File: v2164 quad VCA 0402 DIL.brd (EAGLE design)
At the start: 41.3 x 14.6 mm, 45 parts, among them IC1 TL072JD, IC2 TL072JD, Q1 BA854SW

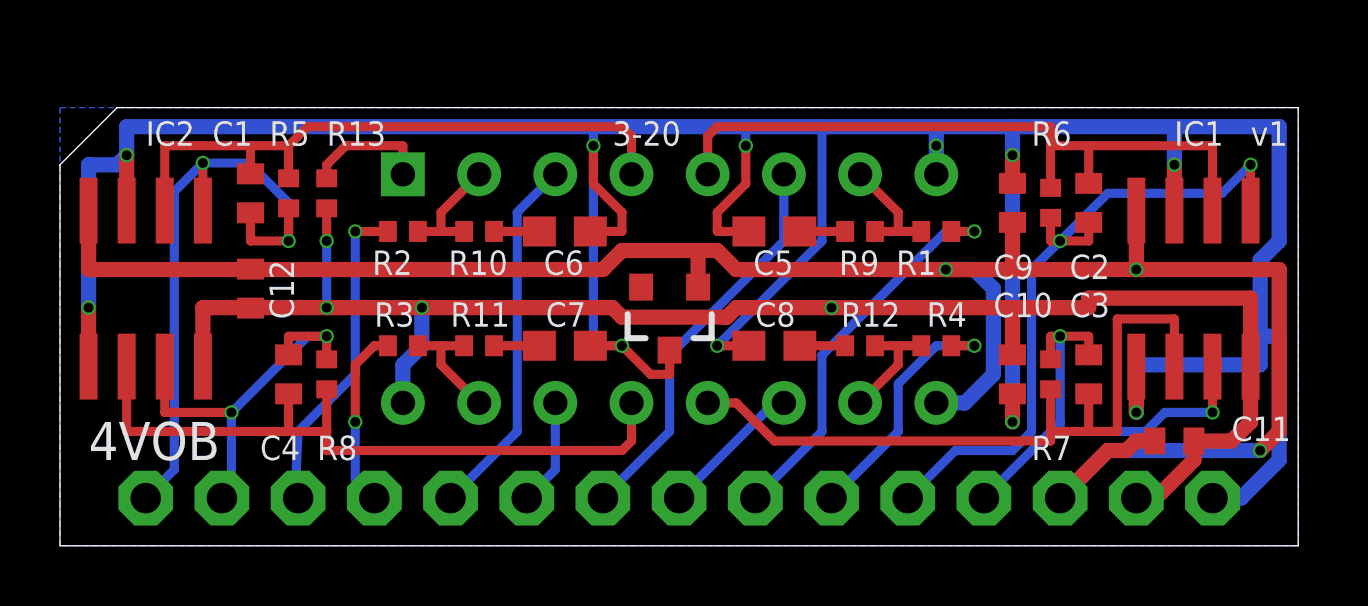
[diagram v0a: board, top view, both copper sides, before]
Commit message: Fixed some silk screen errors and replaced pads with some that solder slightly better
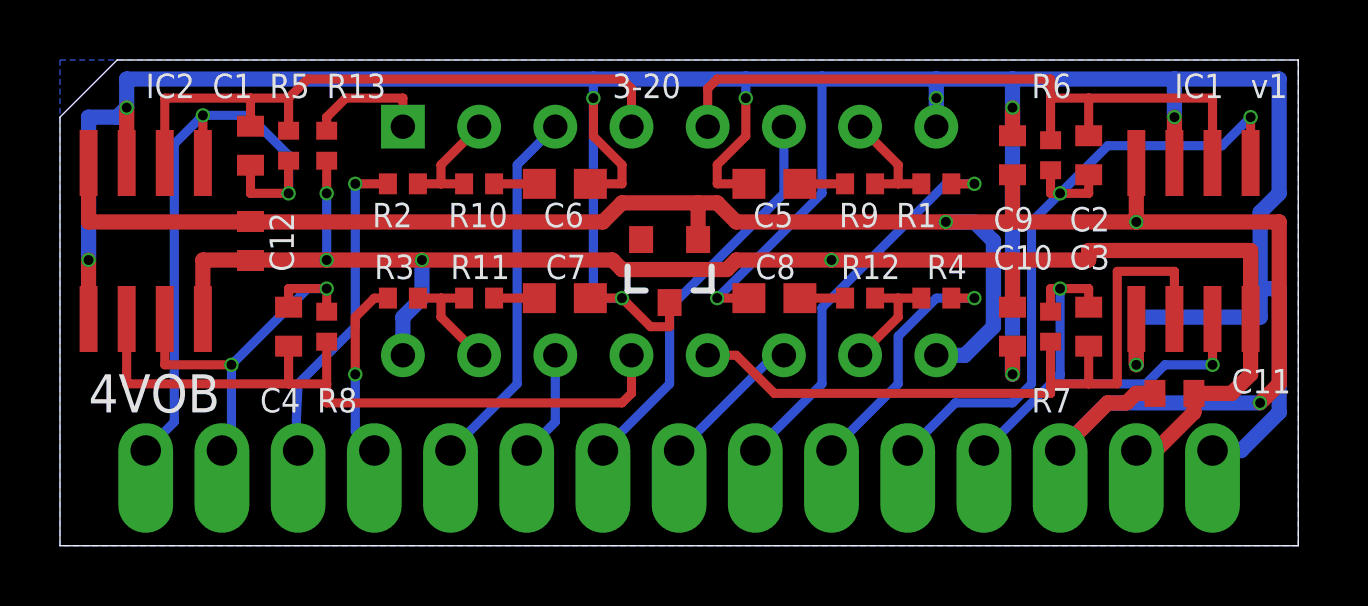
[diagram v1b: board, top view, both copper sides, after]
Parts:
- +15V, -15V, CV1, CV2, CV3, CV4, GND, IN1, IN2, IN3, IN4, OUT1, OUT2, OUT3, OUT4: device joakim:MA01N-1J -> joakim:SIP-PIN01-1J
- moved C1 1.59 mm to (6.35, 13.3)
- moved C10 1.59 mm to (31.8, 7.30)
- moved C12 1.59 mm to (6.35, 10.2)
- moved C2 1.59 mm to (34.3, 13.0)
- moved C3 1.59 mm to (34.3, 7.30)
- moved C4 1.59 mm to (7.62, 7.30)
- moved C5 1.59 mm to (23.8, 12.1)
- moved C6 1.59 mm to (16.8, 12.1)
- moved C7 1.59 mm to (16.8, 8.26)
- moved C8 1.59 mm to (23.8, 8.26)
- moved C9 1.59 mm to (31.8, 13.0)
- moved DA1 1.59 mm to (20.3, 10.2)
- moved IC1 1.59 mm to (37.8, 10.2)
- moved IC2 1.59 mm to (2.86, 10.2)
- moved R1 1.59 mm to (29.2, 12.1)
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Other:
- board size 41.3 x 14.6 mm -> 41.3 x 16.2 mm
- board text added: "Mount socket on this side!"

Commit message: Changed diode to B5817 (1n5817) as BAT854 is not available at JLCPCB
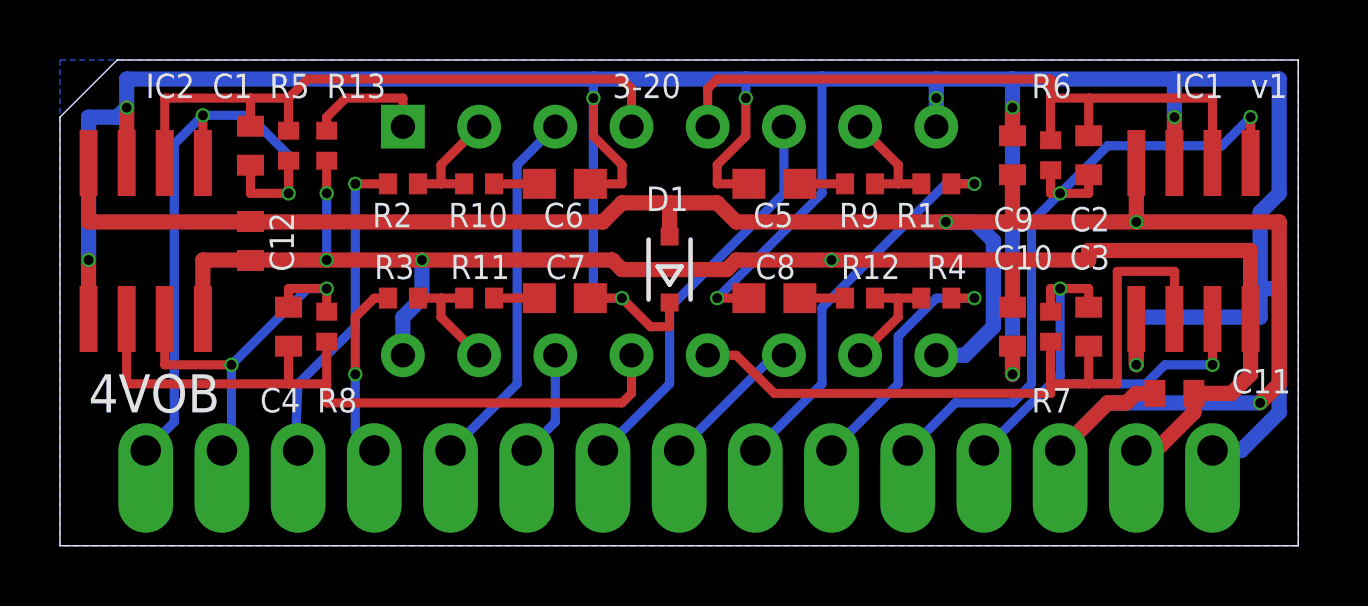
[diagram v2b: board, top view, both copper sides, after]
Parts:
- removed Q1: BA854SW, joakim:SOT23-3J
- added D1: B5817, diode:SOD323-R
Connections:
- net -15V: now also D1.A; no longer Q1.1
- net GND: now also D1.C; no longer Q1.3
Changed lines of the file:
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@@
 <layer number="2" name="Route2" color="16" fill="1" visible="no" active="no"/>
 <layer number="15" name="Route15" color="23" fill="1" visible="no" active="no"/>
-<layer number="16" name="Bottom" color="1" fill="1" visible="yes" active="yes"/>
+<layer number="16" name="Bottom" color="1" fill="1" visible="no" active="yes"/>
 <layer number="17" name="Pads" color="2" fill="1" visible="yes" active="yes"/>
 <layer number="18" name="Vias" color="2" fill="1" visible="yes" active="yes"/>
@@
 <attribute name="VALUE" x="4.445" y="10.795" size="1.27" layer="27" rot="R270"/>
 </element>
-<element name="Q1" library="joakim" package="SOT23-3J" value="BA854SW" x="20.32" y="9.2075" smashed="yes" rot="R180">
-<attribute name="VALUE" x="21.336" y="9.398" size="0.4064" layer="27" rot="R180"/>
-</element>
 <element name="U$1" library="joakim" package="XONIK_LOGO_18" value="" x="29.5275" y="8.3111" smashed="yes" rot="MR0"/>
+<element name="D1" library="diode" library_urn="urn:adsk.eagle:library:210" package="SOD323-R" package3d_urn="urn:adsk.eagle:package:43437/1" value="B5817" x="20.32" y="9.2075" smashed="yes" rot="R90">
+<attribute name="NAME" x="19.5375" y="11.16" size="0.8128" layer="25" font="vector"/>
+<attribute name="POPULARITY" value="4" x="20.32" y="9.2075" size="0.8128" layer="27" font="vector" rot="R90" display="off"/>
+<attribute name="VALUE" x="22.62" y="8.1075" size="1.27" layer="27" rot="R90"/>
+</element>
 </elements>
 <signals>
@@
 <wire x1="40.64" y1="8.5725" x2="40.005" y2="8.5725" width="0.508" layer="16"/>
 <wire x1="35.8775" y1="7.62" x2="35.8775" y2="6.0325" width="0.508" layer="16"/>
-<contactref element="Q1" pad="3"/>
 <wire x1="17.6775" y1="12.065" x2="18.7325" y2="12.065" width="0.3048" layer="1"/>
 <wire x1="18.7325" y1="12.065" x2="18.7325" y2="12.7" width="0.3048" layer="1"/>
@@
 <wire x1="21.9075" y1="12.7" x2="22.86" y2="13.6525" width="0.3048" layer="1"/>
 <via x="22.86" y="14.9225" extent="1-16" drill="0.3302"/>
-<wire x1="20.32" y1="8.1075" x2="20.32" y2="7.3025" width="0.3048" layer="1"/>
-<wire x1="20.32" y1="7.3025" x2="19.685" y2="7.3025" width="0.3048" layer="1"/>
-<wire x1="19.685" y1="7.3025" x2="18.7325" y2="8.255" width="0.3048" layer="1"/>
+<wire x1="18.7325" y1="8.255" x2="19.685" y2="7.3025" width="0.3048" layer="1"/>
 <wire x1="22.86" y1="13.6525" x2="22.86" y2="14.9225" width="0.3048" layer="1"/>
+<contactref element="D1" pad="C"/>
+<wire x1="19.685" y1="7.3025" x2="20.32" y2="7.3025" width="0.3048" layer="1"/>
+<wire x1="20.32" y1="7.3025" x2="20.32" y2="8.1075" width="0.3048" layer="1"/>
 </signal>
 <signal name="N$1">
@@
 <wire x1="29.5275" y1="10.795" x2="22.5425" y2="10.795" width="0.508" layer="1"/>
 <wire x1="22.5425" y1="10.795" x2="21.9075" y2="11.43" width="0.508" layer="1"/>
-<wire x1="21.9075" y1="11.43" x2="21.2725" y2="11.43" width="0.508" layer="1"/>
-<wire x1="21.2725" y1="11.43" x2="18.7325" y2="11.43" width="0.508" layer="1"/>
+<wire x1="20.32" y1="11.43" x2="18.7325" y2="11.43" width="0.508" layer="1"/>
 <wire x1="18.7325" y1="11.43" x2="18.0975" y2="10.795" width="0.508" layer="1"/>
 <wire x1="18.0975" y1="10.795" x2="6.35" y2="10.795" width="0.508" layer="1"/>
@@
 <wire x1="40.64" y1="10.795" x2="35.8775" y2="10.795" width="0.508" layer="1"/>
 <wire x1="34.925" y1="4.7625" x2="33.3375" y2="3.175" width="0.508" layer="16"/>
-<contactref element="Q1" pad="1"/>
 <via x="35.8775" y="10.795" extent="1-16" drill="0.3302"/>
-<wire x1="21.27" y1="10.2075" x2="21.27" y2="11.4275" width="0.508" layer="1"/>
-<wire x1="21.27" y1="11.4275" x2="21.2725" y2="11.43" width="0.508" layer="1"/>
+<contactref element="D1" pad="A"/>
+<wire x1="20.32" y1="10.3075" x2="20.32" y2="11.43" width="0.508" layer="1"/>
+<wire x1="21.9075" y1="11.43" x2="20.32" y2="11.43" width="0.508" layer="1"/>
 </signal>
 <signal name="OUT4">

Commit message: Tiny placement tweak
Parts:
- moved D1 0.32 mm to (20.3, 9.53)
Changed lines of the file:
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@@
 </element>
 <element name="U$1" library="joakim" package="XONIK_LOGO_18" value="" x="29.5275" y="8.3111" smashed="yes" rot="MR0"/>
-<element name="D1" library="diode" library_urn="urn:adsk.eagle:library:210" package="SOD323-R" package3d_urn="urn:adsk.eagle:package:43437/1" value="B5817" x="20.32" y="9.2075" smashed="yes" rot="R90">
-<attribute name="NAME" x="19.5375" y="11.16" size="0.8128" layer="25" font="vector"/>
-<attribute name="POPULARITY" value="4" x="20.32" y="9.2075" size="0.8128" layer="27" font="vector" rot="R90" display="off"/>
-<attribute name="VALUE" x="22.62" y="8.1075" size="1.27" layer="27" rot="R90"/>
+<element name="D1" library="diode" library_urn="urn:adsk.eagle:library:210" package="SOD323-R" package3d_urn="urn:adsk.eagle:package:43437/1" value="B5817" x="20.32" y="9.525" smashed="yes" rot="R90">
+<attribute name="NAME" x="19.5375" y="11.4775" size="0.8128" layer="25" font="vector"/>
+<attribute name="POPULARITY" value="4" x="20.32" y="9.525" size="0.8128" layer="27" font="vector" rot="R90" display="off"/>
+<attribute name="VALUE" x="22.62" y="8.425" size="1.27" layer="27" rot="R90"/>
 </element>
 </elements>
@@
 <wire x1="21.9075" y1="12.7" x2="22.86" y2="13.6525" width="0.3048" layer="1"/>
 <via x="22.86" y="14.9225" extent="1-16" drill="0.3302"/>
-<wire x1="18.7325" y1="8.255" x2="19.685" y2="7.3025" width="0.3048" layer="1"/>
+<wire x1="18.7325" y1="8.255" x2="19.3675" y2="7.62" width="0.3048" layer="1"/>
 <wire x1="22.86" y1="13.6525" x2="22.86" y2="14.9225" width="0.3048" layer="1"/>
 <contactref element="D1" pad="C"/>
-<wire x1="19.685" y1="7.3025" x2="20.32" y2="7.3025" width="0.3048" layer="1"/>
-<wire x1="20.32" y1="7.3025" x2="20.32" y2="8.1075" width="0.3048" layer="1"/>
+<wire x1="19.3675" y1="7.62" x2="20.32" y2="7.62" width="0.3048" layer="1"/>
+<wire x1="20.32" y1="7.62" x2="20.32" y2="8.425" width="0.3048" layer="1"/>
 </signal>
 <signal name="N$1">
@@
 <wire x1="34.29" y1="9.525" x2="31.75" y2="9.525" width="0.508" layer="1"/>
 <wire x1="31.75" y1="9.525" x2="25.7175" y2="9.525" width="0.508" layer="1"/>
-<wire x1="25.7175" y1="9.525" x2="22.5425" y2="9.525" width="0.508" layer="1"/>
-<wire x1="22.5425" y1="9.525" x2="22.225" y2="9.2075" width="0.508" layer="1"/>
-<wire x1="22.225" y1="9.2075" x2="18.7325" y2="9.2075" width="0.508" layer="1"/>
-<wire x1="18.7325" y1="9.2075" x2="18.415" y2="9.525" width="0.508" layer="1"/>
-<wire x1="18.415" y1="9.525" x2="12.065" y2="9.525" width="0.508" layer="1"/>
+<wire x1="25.7175" y1="9.525" x2="12.065" y2="9.525" width="0.508" layer="1"/>
 <wire x1="12.065" y1="9.525" x2="8.89" y2="9.525" width="0.508" layer="1"/>
 <wire x1="8.89" y1="9.525" x2="6.35" y2="9.525" width="0.508" layer="1"/>
@@
 <contactref element="C12" pad="1"/>
 <wire x1="31.75" y1="10.795" x2="29.5275" y2="10.795" width="0.508" layer="1"/>
-<wire x1="29.5275" y1="10.795" x2="22.5425" y2="10.795" width="0.508" layer="1"/>
-<wire x1="22.5425" y1="10.795" x2="21.9075" y2="11.43" width="0.508" layer="1"/>
-<wire x1="20.32" y1="11.43" x2="18.7325" y2="11.43" width="0.508" layer="1"/>
-<wire x1="18.7325" y1="11.43" x2="18.0975" y2="10.795" width="0.508" layer="1"/>
-<wire x1="18.0975" y1="10.795" x2="6.35" y2="10.795" width="0.508" layer="1"/>
+<wire x1="29.5275" y1="10.795" x2="21.9075" y2="10.795" width="0.508" layer="1"/>
+<wire x1="21.9075" y1="10.795" x2="21.2725" y2="11.43" width="0.508" layer="1"/>
+<wire x1="20.32" y1="11.43" x2="19.3675" y2="11.43" width="0.508" layer="1"/>
+<wire x1="19.3675" y1="11.43" x2="18.7325" y2="10.795" width="0.508" layer="1"/>
+<wire x1="18.7325" y1="10.795" x2="6.35" y2="10.795" width="0.508" layer="1"/>
 <wire x1="6.35" y1="10.795" x2="0.9525" y2="10.795" width="0.508" layer="1"/>
 <wire x1="29.5275" y1="10.795" x2="30.48" y2="10.795" width="0.508" layer="16"/>
@@
 <via x="35.8775" y="10.795" extent="1-16" drill="0.3302"/>
 <contactref element="D1" pad="A"/>
-<wire x1="20.32" y1="10.3075" x2="20.32" y2="11.43" width="0.508" layer="1"/>
-<wire x1="21.9075" y1="11.43" x2="20.32" y2="11.43" width="0.508" layer="1"/>
+<wire x1="20.32" y1="10.625" x2="20.32" y2="11.43" width="0.508" layer="1"/>
+<wire x1="21.2725" y1="11.43" x2="20.32" y2="11.43" width="0.508" layer="1"/>
 </signal>
 <signal name="OUT4">
